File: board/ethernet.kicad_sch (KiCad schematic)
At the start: 26 parts, among them U4 LAN8742A, U5 USBLC6-4SC6, X1 NX2016SA-25.000M-STD-CZS-1

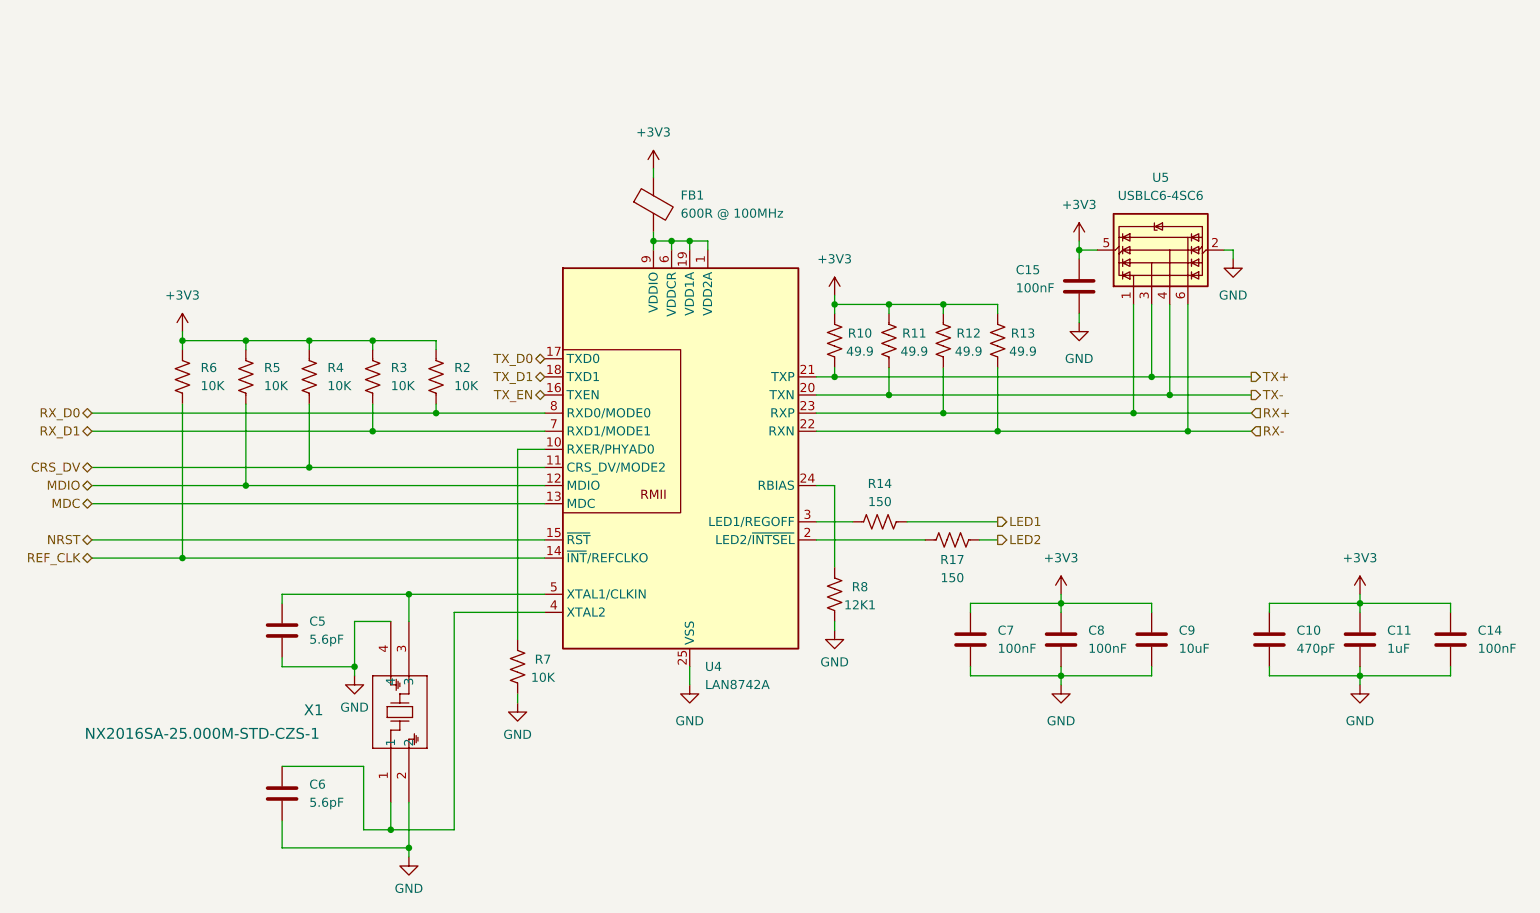
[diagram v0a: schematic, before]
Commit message: Replaced buck with AP2303, fixed PHY schematic
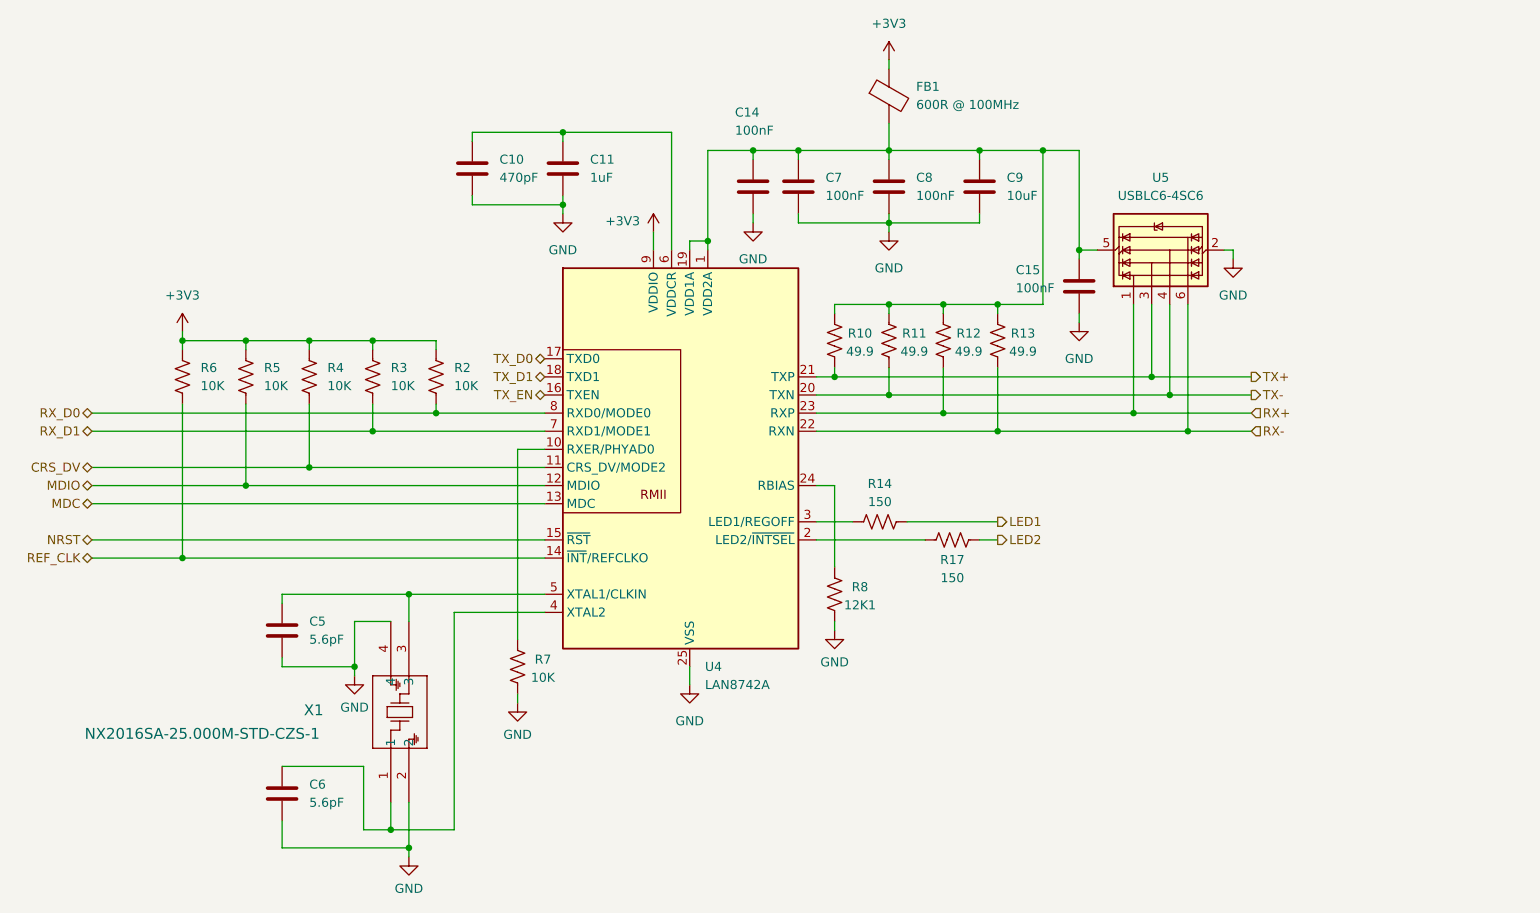
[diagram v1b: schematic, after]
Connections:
- net +3V3: now also U4.9 (VDDIO); no longer C10.1, C11.1, C14.1, C15.1, C7.1, C8.1, C9.1, R10.1, R11.1, R12.1, R13.1, U5.5 (VBUS)
- net at FB1.2, U4.1 (VDD2A), U4.19 (VDD1A): now also C14.1, C15.1, C7.1, C8.1, C9.1, R10.1, R11.1, R12.1, R13.1, U5.5 (VBUS); no longer U4.6 (VDDCR), U4.9 (VDDIO)
- new net: C10.1, C11.1, U4.6 (VDDCR)
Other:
- moved on the sheet: C10, C11, C14, C7, C8, C9, FB1

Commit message: Schematic and Layout Complete
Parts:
- added R18: 10K, Resistor_SMD:R_0603_1608Metric_Pad0.98x0.95mm_HandSolder, symbol Device:R_US
- added R20, R21: 10k, Resistor_SMD:R_0603_1608Metric_Pad0.98x0.95mm_HandSolder, symbol Device:R_US
- R5: value 10K -> 1k5
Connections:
- net +3V3: now also R18.2
- net GND: now also R20.2, R21.2
- net NRST: now also R18.1
- net at R17.1, U4.2 (LED2/~{INTSEL}): now also R20.1
- net at R14.1, U4.3 (LED1/REGOFF): now also R21.1
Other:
- moved on the sheet: R14, R17
